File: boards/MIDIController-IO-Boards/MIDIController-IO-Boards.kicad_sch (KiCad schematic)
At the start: 25 parts, among them J10 I2C, J11 LTC4311_1, J12 IO_Boards, J13 I2C2, J14 DC12V, J15 LTC4311_2, J5 I2CAddr, J8 TCA9548A 1, J9 TCA9548A 2, U1 LME78_05-1.0

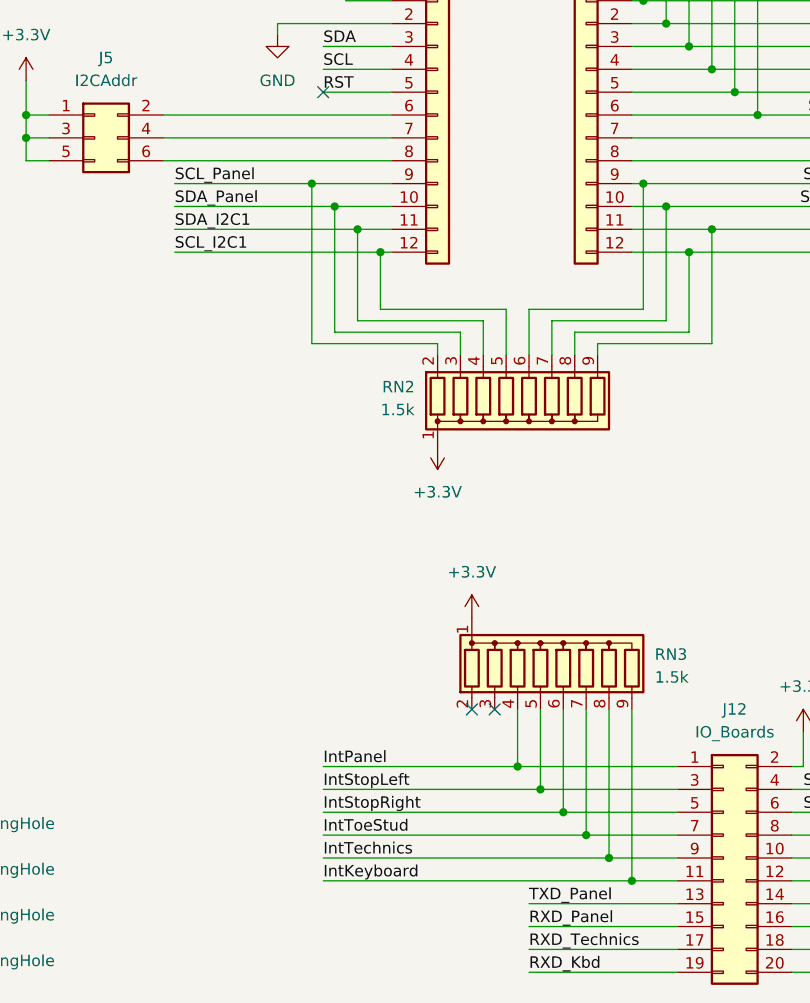
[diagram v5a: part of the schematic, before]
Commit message: Fixed some RX/TX pin swaps
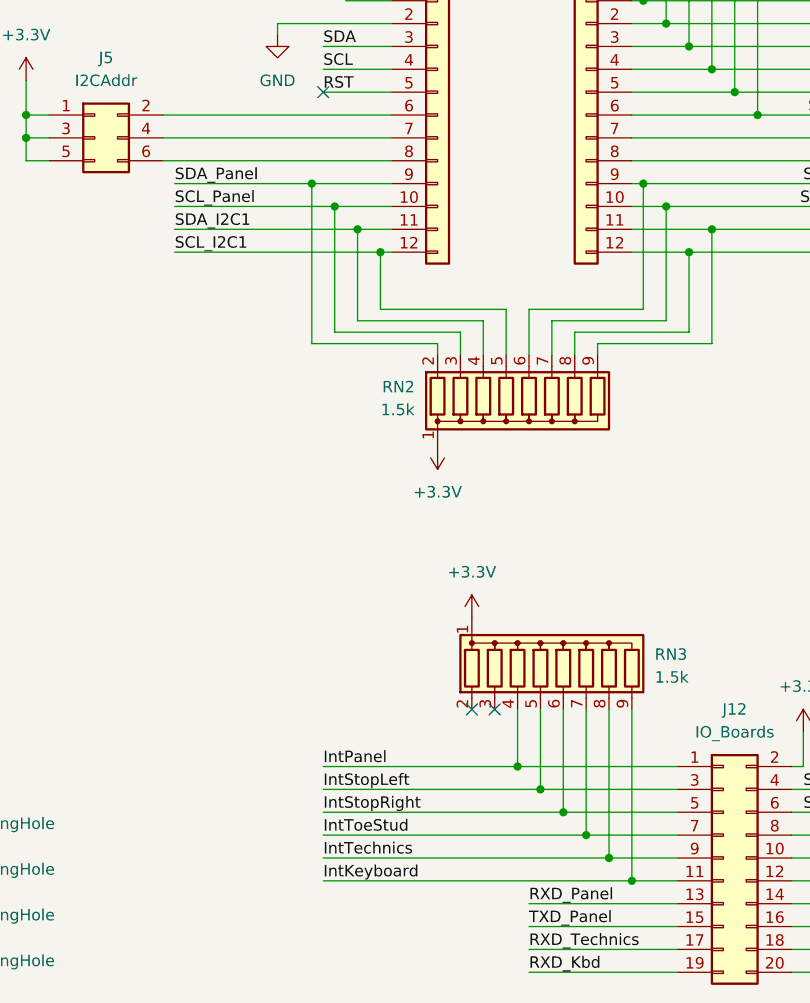
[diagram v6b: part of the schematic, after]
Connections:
- net RXD_Panel: now also J12.13 (Pin_13); no longer J12.15 (Pin_15)
- net SCL_Panel: now also J8.10 (Pin_10), RN2.3 (R2); no longer J8.9 (Pin_9), RN2.2 (R1)
- net SDA_Panel: now also J8.9 (Pin_9), RN2.2 (R1); no longer J8.10 (Pin_10), RN2.3 (R2)
- net TXD_Panel: now also J12.15 (Pin_15); no longer J12.13 (Pin_13)
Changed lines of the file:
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@@
 	)
 	(label "SDA_Panel"
-		(at 48.26 101.6 0)
+		(at 48.26 99.06 0)
 		(fields_autoplaced yes)
 		(effects
@@
 	)
 	(label "TXD_Panel"
-		(at 87.63 179.07 0)
+		(at 87.63 181.61 0)
 		(fields_autoplaced yes)
 		(effects
@@
 	)
 	(label "RXD_Panel"
-		(at 87.63 181.61 0)
+		(at 87.63 179.07 0)
 		(fields_autoplaced yes)
 		(effects
@@
 	)
 	(label "SCL_Panel"
-		(at 48.26 99.06 0)
-		(fields_autoplaced yes)
-		(effects
+		(at 48.26 101.6 0)
+		(fields_autoplaced yes)
+		(effects

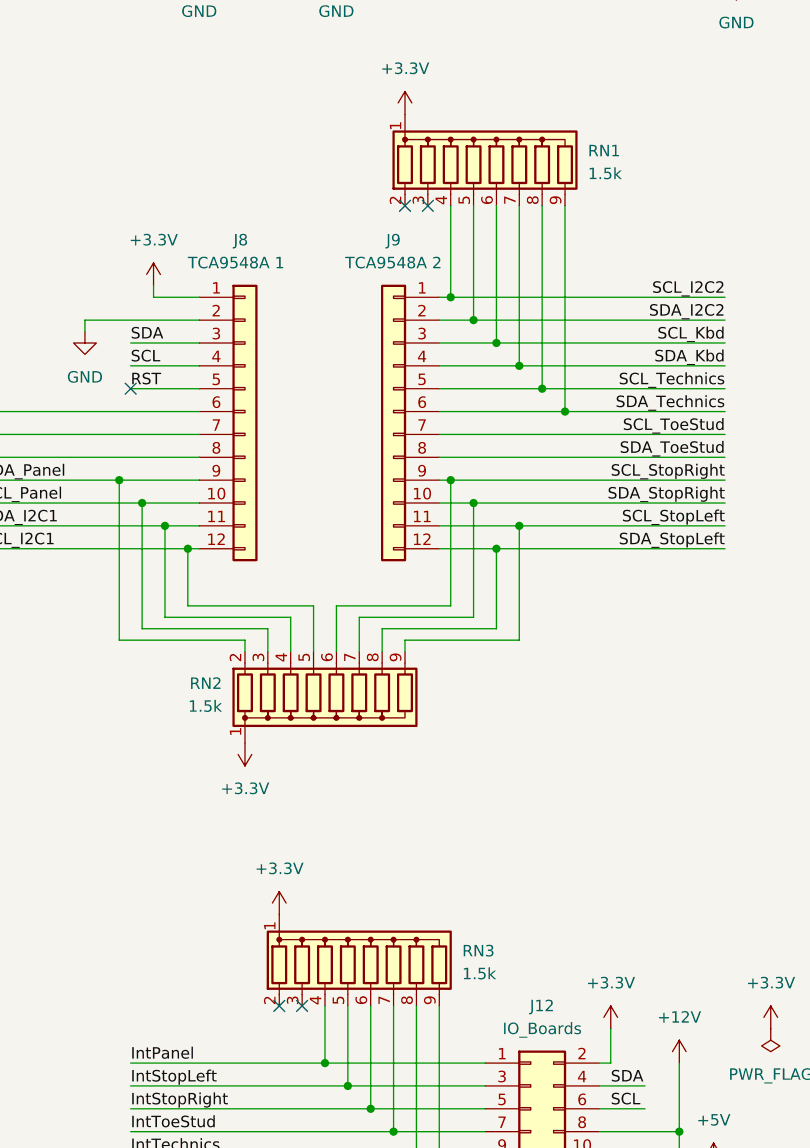
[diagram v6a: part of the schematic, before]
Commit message: Fixed size of I2C expander board footprint
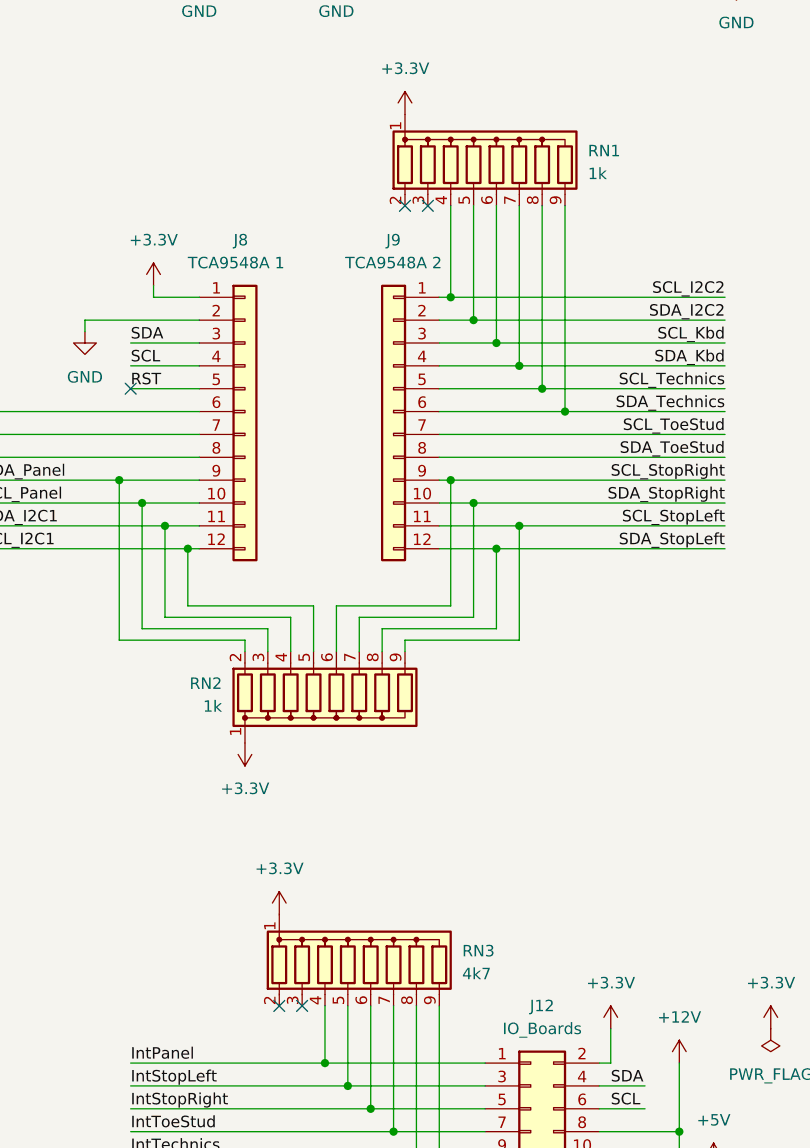
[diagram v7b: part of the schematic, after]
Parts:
- RN1, RN2: value 1.5k -> 1k
- RN3: value 1.5k -> 4k7
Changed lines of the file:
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@@
 			)
 		)
-		(property "Value" "1.5k"
+		(property "Value" "1k"
 			(at 74.93 124.2059 0)
 			(effects
@@
 			)
 		)
-		(property "Value" "1.5k"
+		(property "Value" "4k7"
 			(at 101.6 153.9239 0)
 			(effects
@@
 			)
 		)
-		(property "Value" "1.5k"
+		(property "Value" "1k"
 			(at 115.57 65.0239 0)
 			(effects
